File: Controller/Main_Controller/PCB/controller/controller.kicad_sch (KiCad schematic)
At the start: 252 parts, among them J1 Conn_01x10, M1 Motor_DC, Q1 BC817, Q10 BC817, Q11 BC817, Q12 BC817, Q13 BC817, Q14 BC817, Q15 BC817, Q16 BC817, Q17 BC817, Q18 BC817, Q19 BC817, Q2 BC817, Q20 BC817, Q21 BC817, Q22 BC817, Q23 BC817, Q24 BC817, Q25 IRFR9014PBF, Q26 STD20NF06L, Q3 BC817, Q31 BC817, Q4 BC817, Q5 BC817, Q6 BC817, Q7 BC817, Q8 BC817, Q9 BC817, SW1 SW_SPDT, SW2 SW_SPDT, U1 NUCLEO-L432KC, U10 ZLDO1117G50TA, U2 NUCLEO144-F429ZI, U3 74HC14, U4 74HC14, U5 74HC14, U6 Joystick, U7 Joystick, U8 HY1602E, U9 ZSR330GTA

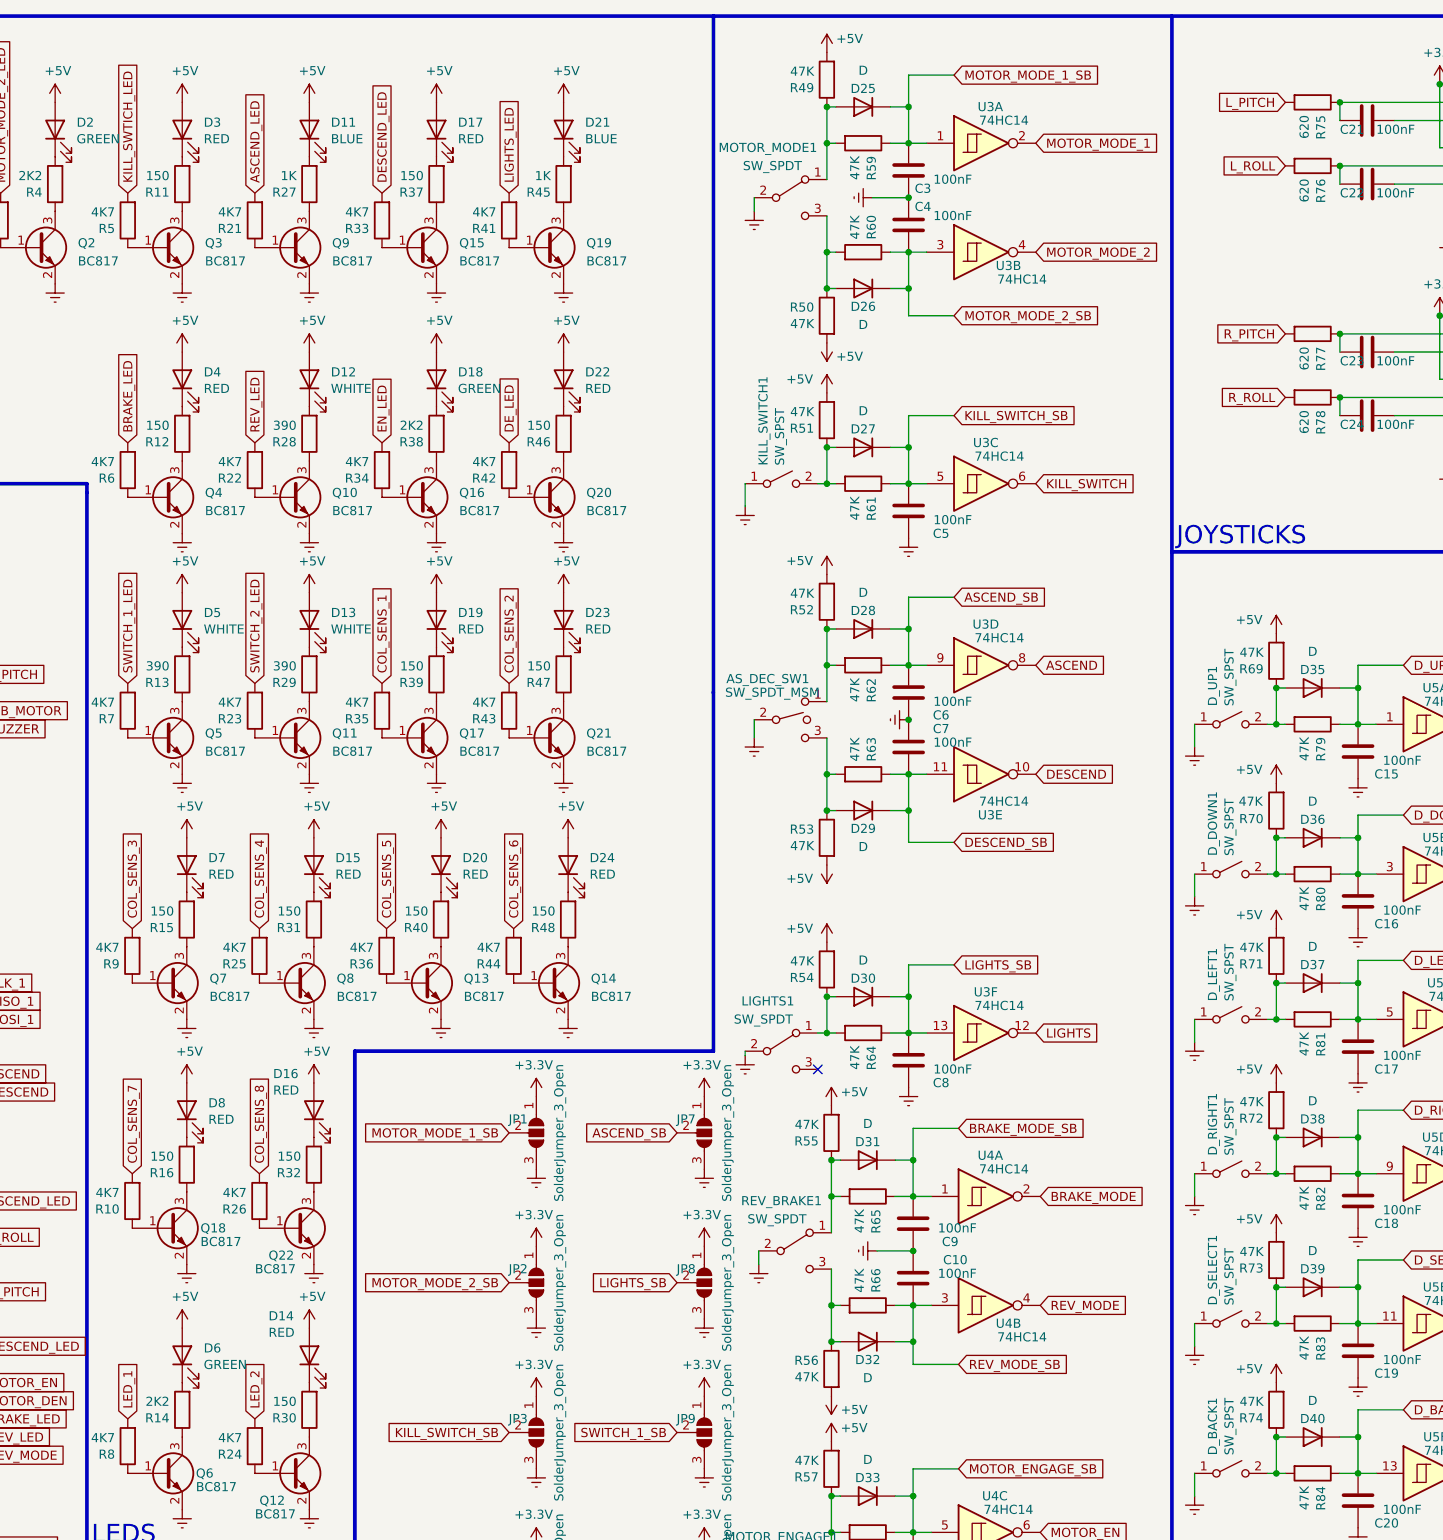
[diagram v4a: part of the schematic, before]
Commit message: LCD footprint and created BOM.
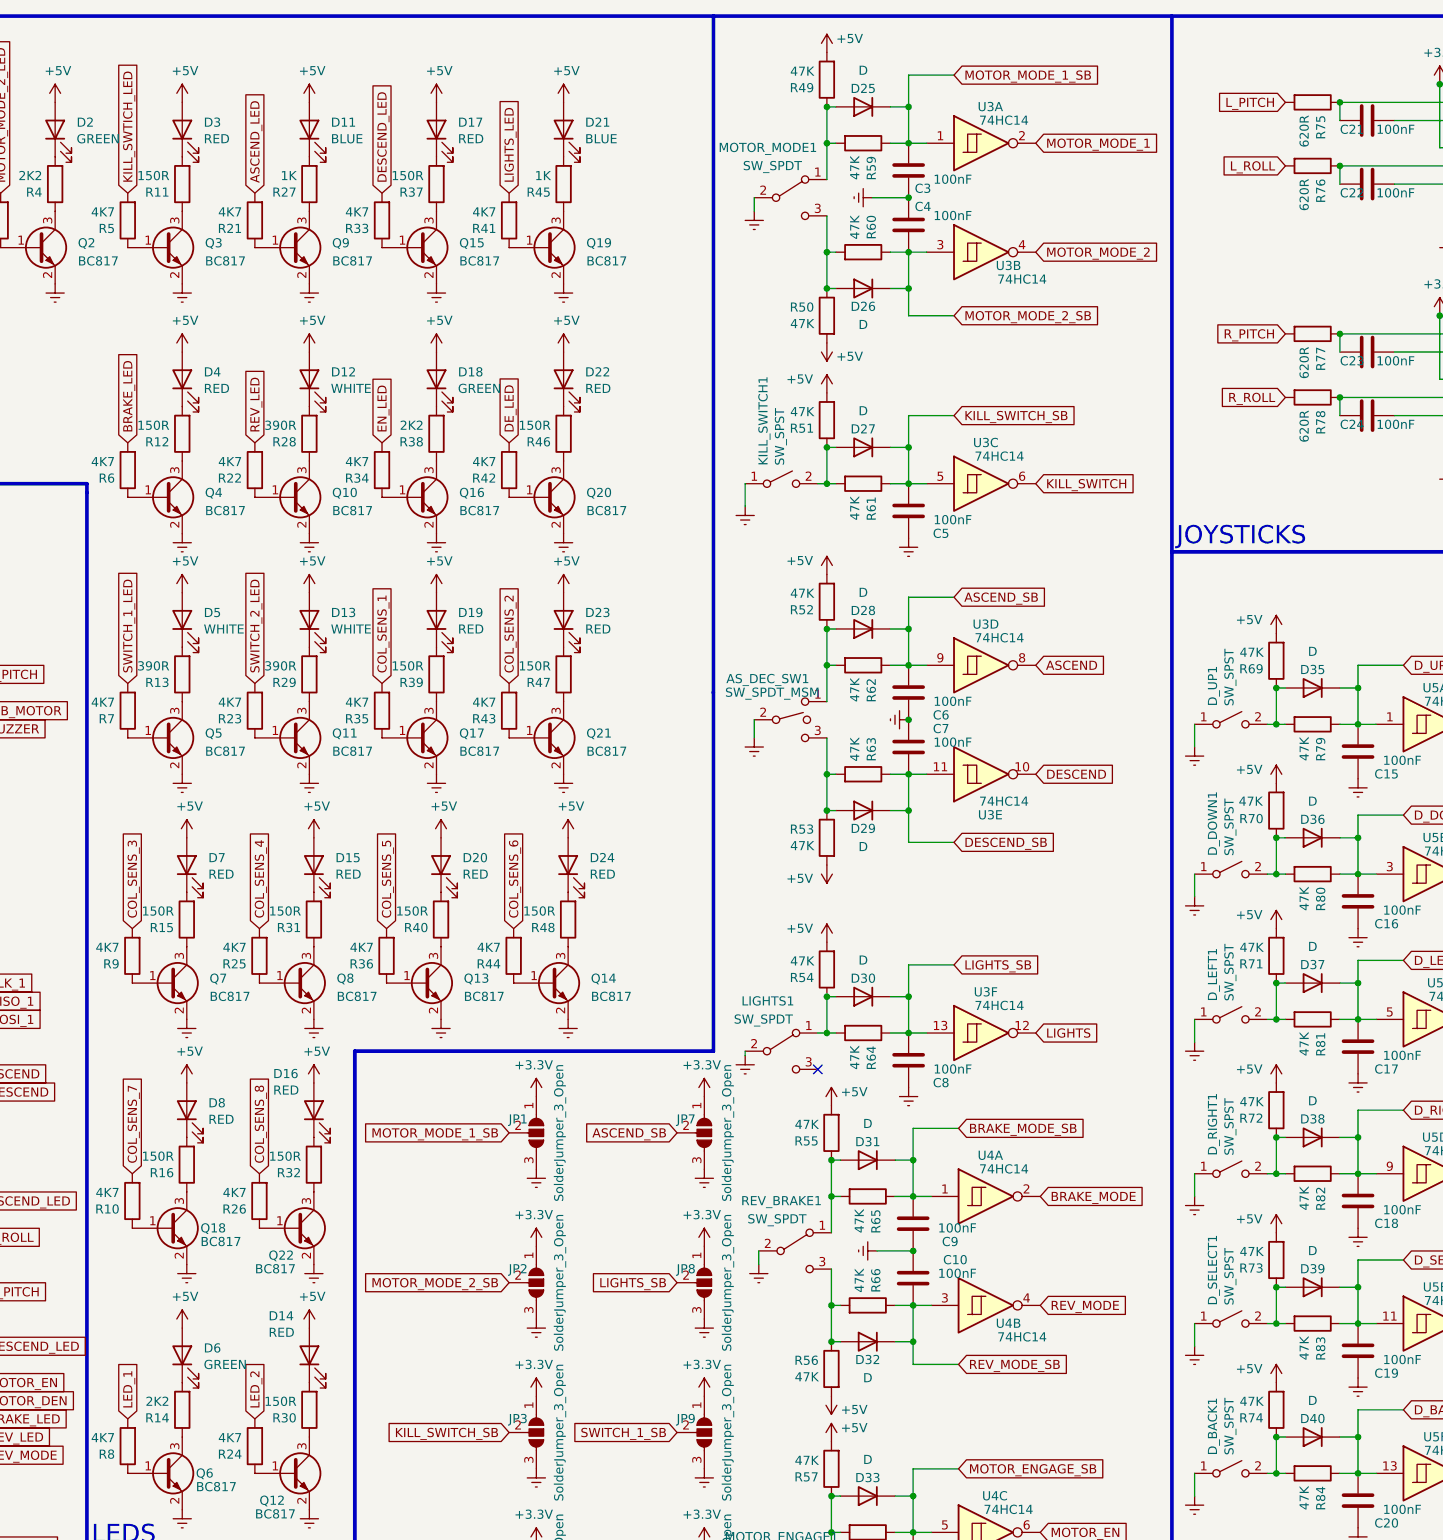
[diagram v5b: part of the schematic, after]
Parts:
- R11, R12, R15, R16, R30, R31, R32, R37, R39, R40, R46, R47, R48: value 150 -> 150R
- R13, R28, R29: value 390 -> 390R
- R75, R76, R77, R78: value 620 -> 620R
- U8: footprint Display:HY1602E -> My_library:LCD_Display_WH1602B-NYG-JT
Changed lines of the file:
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@@
       (effects (font (size 1.27 1.27)) (justify left))
     )
-    (property "Value" "620" (at 278.892 25.908 0)
+    (property "Value" "620R" (at 278.892 25.908 0)
       (effects (font (size 1.27 1.27)) (justify left))
     )
@@
       (effects (font (size 1.27 1.27)) (justify left))
     )
-    (property "Value" "150" (at 120.777 171.577 0)
+    (property "Value" "150R" (at 120.777 171.577 0)
       (effects (font (size 1.27 1.27)) (justify left))
     )
@@
       (effects (font (size 1.27 1.27)) (justify left))
     )
-    (property "Value" "620" (at 278.892 34.798 0)
+    (property "Value" "620R" (at 278.892 34.798 0)
       (effects (font (size 1.27 1.27)) (justify left))
     )
@@
       (effects (font (size 1.27 1.27)) (justify left))
     )
-    (property "Value" "390" (at 137.922 102.997 0)
+    (property "Value" "390R" (at 137.922 102.997 0)
       (effects (font (size 1.27 1.27)) (justify left))
     )
@@
       (effects (font (size 1.27 1.27)) (justify left))
     )
-    (property "Value" "150" (at 174.117 137.287 0)
+    (property "Value" "150R" (at 174.117 137.287 0)
       (effects (font (size 1.27 1.27)) (justify left))
     )
@@
       (effects (font (size 1.27 1.27)) (justify left))
     )
-    (property "Value" "150" (at 138.557 171.577 0)
+    (property "Value" "150R" (at 138.557 171.577 0)
       (effects (font (size 1.27 1.27)) (justify left))
     )
@@
       (effects (font (size 1.27 1.27)) (justify left))
     )
-    (property "Value" "620" (at 278.892 67.183 0)
+    (property "Value" "620R" (at 278.892 67.183 0)
       (effects (font (size 1.27 1.27)) (justify left))
     )
@@
       (effects (font (size 1.27 1.27)) (justify left))
     )
-    (property "Value" "150" (at 156.337 137.287 0)
+    (property "Value" "150R" (at 156.337 137.287 0)
       (effects (font (size 1.27 1.27)) (justify left))
     )
@@
       (effects (font (size 1.27 1.27)) (justify left))
     )
-    (property "Value" "150" (at 155.702 102.997 0)
+    (property "Value" "150R" (at 155.702 102.997 0)
       (effects (font (size 1.27 1.27)) (justify left))
     )
@@
       (effects (font (size 1.27 1.27)) (justify left))
     )
-    (property "Footprint" "Display:HY1602E" (at 370.205 247.65 0)
+    (property "Footprint" "My_library:LCD_Display_WH1602B-NYG-JT" (at 370.205 247.65 0)
       (effects (font (size 1.27 1.27) italic) hide)
     )
@@
       (effects (font (size 1.27 1.27)) (justify left))
     )
-    (property "Value" "150" (at 138.557 137.287 0)
+    (property "Value" "150R" (at 138.557 137.287 0)
       (effects (font (size 1.27 1.27)) (justify left))
     )
@@
       (effects (font (size 1.27 1.27)) (justify left))
     )
-    (property "Value" "150" (at 155.702 34.417 0)
+    (property "Value" "150R" (at 155.702 34.417 0)
       (effects (font (size 1.27 1.27)) (justify left))
     )
@@
       (effects (font (size 1.27 1.27)) (justify left))
     )
-    (property "Value" "620" (at 278.892 58.293 0)
+    (property "Value" "620R" (at 278.892 58.293 0)
       (effects (font (size 1.27 1.27)) (justify left))
     )
@@
       (effects (font (size 1.27 1.27)) (justify left))
     )
-    (property "Value" "150" (at 120.142 34.417 0)
+    (property "Value" "150R" (at 120.142 34.417 0)
       (effects (font (size 1.27 1.27)) (justify left))
     )
@@
       (effects (font (size 1.27 1.27)) (justify left))
     )
-    (property "Value" "150" (at 137.922 205.867 0)
+    (property "Value" "150R" (at 137.922 205.867 0)
       (effects (font (size 1.27 1.27)) (justify left))
     )
@@
       (effects (font (size 1.27 1.27)) (justify left))
     )
-    (property "Value" "390" (at 120.142 102.997 0)
+    (property "Value" "390R" (at 120.142 102.997 0)
       (effects (font (size 1.27 1.27)) (justify left))
     )
@@
       (effects (font (size 1.27 1.27)) (justify left))
     )
-    (property "Value" "150" (at 120.777 137.287 0)
+    (property "Value" "150R" (at 120.777 137.287 0)
       (effects (font (size 1.27 1.27)) (justify left))
     )
@@
       (effects (font (size 1.27 1.27)) (justify left))
     )
-    (property "Value" "150" (at 173.482 102.997 0)
+    (property "Value" "150R" (at 173.482 102.997 0)
       (effects (font (size 1.27 1.27)) (justify left))
     )
@@
       (effects (font (size 1.27 1.27)) (justify left))
     )
-    (property "Value" "150" (at 173.482 69.342 0)
+    (property "Value" "150R" (at 173.482 69.342 0)
       (effects (font (size 1.27 1.27)) (justify left))
     )
@@
       (effects (font (size 1.27 1.27)) (justify left))
     )
-    (property "Value" "390" (at 137.922 69.342 0)
+    (property "Value" "390R" (at 137.922 69.342 0)
       (effects (font (size 1.27 1.27)) (justify left))
     )
@@
       (effects (font (size 1.27 1.27)) (justify left))
     )
-    (property "Value" "150" (at 120.142 69.342 0)
+    (property "Value" "150R" (at 120.142 69.342 0)
       (effects (font (size 1.27 1.27)) (justify left))
     )

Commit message: PCB design
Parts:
- KILL_SWITCH1: footprint Button_Switch_SMD:SW_Push_1P1T_NO_6x6mm_H9.5mm -> My_library:Toggle_Switch_10TC605
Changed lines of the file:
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@@
       (effects (font (size 1.27 1.27)) (justify left))
     )
-    (property "Footprint" "Button_Switch_SMD:SW_Push_1P1T_NO_6x6mm_H9.5mm" (at 205.74 77.47 0)
+    (property "Footprint" "My_library:Toggle_Switch_10TC605" (at 205.74 77.47 0)
       (effects (font (size 1.27 1.27)) hide)
     )

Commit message: Tracings complete for the PCB.
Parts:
- removed KILL_SWITCH1: SW_SPST, My_library:Toggle_Switch_10TC605, symbol Switch:SW_SPST
- added JP19: Jumper_2_Open, symbol Jumper:Jumper_2_Open
- added JP20: SolderJumper_2_Open, symbol Jumper:SolderJumper_2_Open
- added KILL_SWITCH1: SW_SPDT, My_library:1Ms1T1B1M1QE, symbol Switch:SW_SPDT
- R93, R95, R97: footprint Resistor_SMD:R_0201_0603Metric -> Resistor_SMD:R_0603_1608Metric
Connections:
- net D_SELECT is gone; now on net D_SEL: U1.15 (D12)
- net KILL_SWTICH_LED is gone; now on net KILL_LED: R5.2
- net MOTOR_DEN is gone; now on net KILL_LED: U2.73 (PC9)
- net ASCEND: now also U2.77 (PB9); no longer U2.75 (PB8)
- net BRAKE_LED: now also U2.2 (PC11); no longer U2.1 (PC10)
- net COL_SENS_1: now also U2.116 (PE7); no longer U2.137 (PD10)
- net COL_SENS_2: now also U2.115 (PD12); no longer U2.117 (PD11)
- net COL_SENS_3: now also U2.119 (PE10); no longer U2.125 (PE15)
- net COL_SENS_4: now also U2.117 (PD11); no longer U2.123 (PE14)
- net COL_SENS_5: now also U2.123 (PE14); no longer U2.128 (PE11)
- net COL_SENS_6: now also U2.125 (PE15); no longer U2.119 (PE10)
- net COL_SENS_8: now also U2.128 (PE11); no longer U2.116 (PE7)
- net DESCEND: now also U2.75 (PB8); no longer U2.77 (PB9)
- net Earth: now also KILL_SWITCH1.2 (B)
- net KILL_LED: no longer U2.108 (PF5)
- net KILL_SWITCH: now also U2.74 (PC8); no longer U2.114 (PF10)
- net L_PITCH: now also U2.37 (PC3); no longer U2.109 (PA3)
- net L_ROLL: now also U2.130 (PF3); no longer U2.38 (PC0)
- net MOTOR_DE: now also U2.108 (PF5)
- net MOTOR_EN: now also U2.114 (PF10); no longer U2.74 (PC8)
- net REV_LED: now also U2.1 (PC10); no longer U2.2 (PC11)
- net R_PITCH: now also U2.38 (PC0); no longer U2.37 (PC3)
- net R_ROLL: now also U2.109 (PA3); no longer U2.130 (PF3)
- net at D27.2 (A), R51.1, R61.2: now also KILL_SWITCH1.1 (A)
- net DET_IN: no longer names the net of J1.8 (Pin_8)
- net DET_IN: now also JP19.2 (B), JP20.2 (B)
- net DET_OUT: no longer names the net of J1.9 (Pin_9)
- net DET_OUT: now also JP19.1 (A), JP20.1 (A)
- no-connect marks 101 -> 102

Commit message: Edge and earth added to the PCB.
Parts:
- JP19: footprint (none) -> My_library:Jumper
- JP20: footprint (none) -> Jumper:SolderJumper-2_P1.3mm_Open_RoundedPad1.0x1.5mm
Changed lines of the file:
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@@
       (effects (font (size 1.27 1.27)) (justify right))
     )
-    (property "Footprint" "" (at 267.97 273.685 0)
+    (property "Footprint" "Jumper:SolderJumper-2_P1.3mm_Open_RoundedPad1.0x1.5mm" (at 267.97 273.685 0)
       (effects (font (size 1.27 1.27)) hide)
     )
@@
       (effects (font (size 1.27 1.27)) (justify right))
     )
-    (property "Footprint" "" (at 278.13 273.685 0)
-      (effects (font (size 1.27 1.27)) hide)
-    )
+    (property "Footprint" "My_library:Jumper" (at 278.13 273.685 0)
+      (effects (font (size 1.27 1.27)) hide)
+    )
